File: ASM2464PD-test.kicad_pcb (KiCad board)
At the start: 4 copper layers, 81.8 x 19 mm, 87 parts, among them J1 USB_C_Receptacle, J2 SPIheader, J3 Bus_PCI_Express_x4, U2 SPI_SOIC-8, U3 SPI_DFN-8, Y1 25MHz

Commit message: Very bad routing lol
should probably not try to make it *that* compact
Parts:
- added J4: chip-annoyers, Connector_PinHeader_2.54mm:PinHeader_2x02_P2.54mm_Vertical, F.Cu at (161.5, 60.1)
- added J5: UART, Connector_PinHeader_2.54mm:PinHeader_1x04_P2.54mm_Vertical, F.Cu at (173.2, 50.7)
- added J6: I2C, Connector_PinHeader_2.54mm:PinHeader_1x04_P2.54mm_Vertical, F.Cu at (177.8, 50.7)
- C10, R3, R4, R5, R6: moved to F.Cu
- D1: renamed from D3; moved to F.Cu
- D2: renamed from D4; moved to F.Cu
- D3: renamed from D5; moved to F.Cu
- D4: renamed from D6; moved to F.Cu
- moved R3 161.0 mm to (199.0, 108.0), turned to 180 degrees
- moved R4 160.6 mm to (199.0, 107.0), turned to 180 degrees
- moved R6 154.7 mm to (192.8, 107.6), turned to 180 degrees
- moved R5 154.5 mm to (192.8, 106.6), turned to 180 degrees
- moved R8 148.1 mm to (204.0, 106.0), turned to 180 degrees
- moved R7 148.1 mm to (204.0, 107.0), turned to 180 degrees
- moved C10 126.1 mm to (183.7, 120.8)
- moved R10 81.3 mm to (183.1, 119.2)
- moved R9 81.3 mm to (183.1, 117.4)
- moved Y1 65.4 mm to (172.6, 111.4)
- moved C1 63.4 mm to (172.7, 114.7)
- moved C7 62.2 mm to (190.8, 96.2), turned to 180 degrees
- moved C6 60.6 mm to (190.8, 96.8), turned to 180 degrees
- moved C5 57.6 mm to (190.8, 101.6), turned to 180 degrees
- moved C4 56.9 mm to (190.8, 101.0), turned to 180 degrees
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- renumbered D2 to D10, D7 to D5, D8 to D6, D9 to D7, D10 to D8, D1 to D9
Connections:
- U1 pad H21: unconnected-(U1A-TEST_EN-PadH21) -> TEST_EN
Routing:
- net PCIe_RX3-: track 1.60 -> 36.9 mm, vias 0 -> 1
- net PCIe_RX3+: track 1.66 -> 36.3 mm, vias 0 -> 1
- net /Main/UTX1_C+: track 0.00 -> 18.9 mm, vias 0 -> 2
- net /Main/UTX1_C-: track 0.00 -> 18.9 mm, vias 0 -> 2
- net /Main/URX0_C-: track 0.00 -> 18.8 mm, vias 0 -> 2
- net /Main/URX0_C+: track 0.00 -> 18.8 mm, vias 0 -> 2
- net UTX0-: track 0.00 -> 13.9 mm
- net UTX0+: track 0.00 -> 13.3 mm
- net URX1+: track 0.00 -> 11.9 mm
- net URX1-: track 0.00 -> 11.4 mm
- net /Main/UTX0_C-: track 0.00 -> 7.08 mm
- net /Main/UTX0_C+: track 0.00 -> 7.08 mm
- net URX0-: track 0.00 -> 7.03 mm
- net /Main/URX1_C-: track 0.00 -> 6.92 mm
- net /Main/URX1_C+: track 0.00 -> 6.92 mm
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
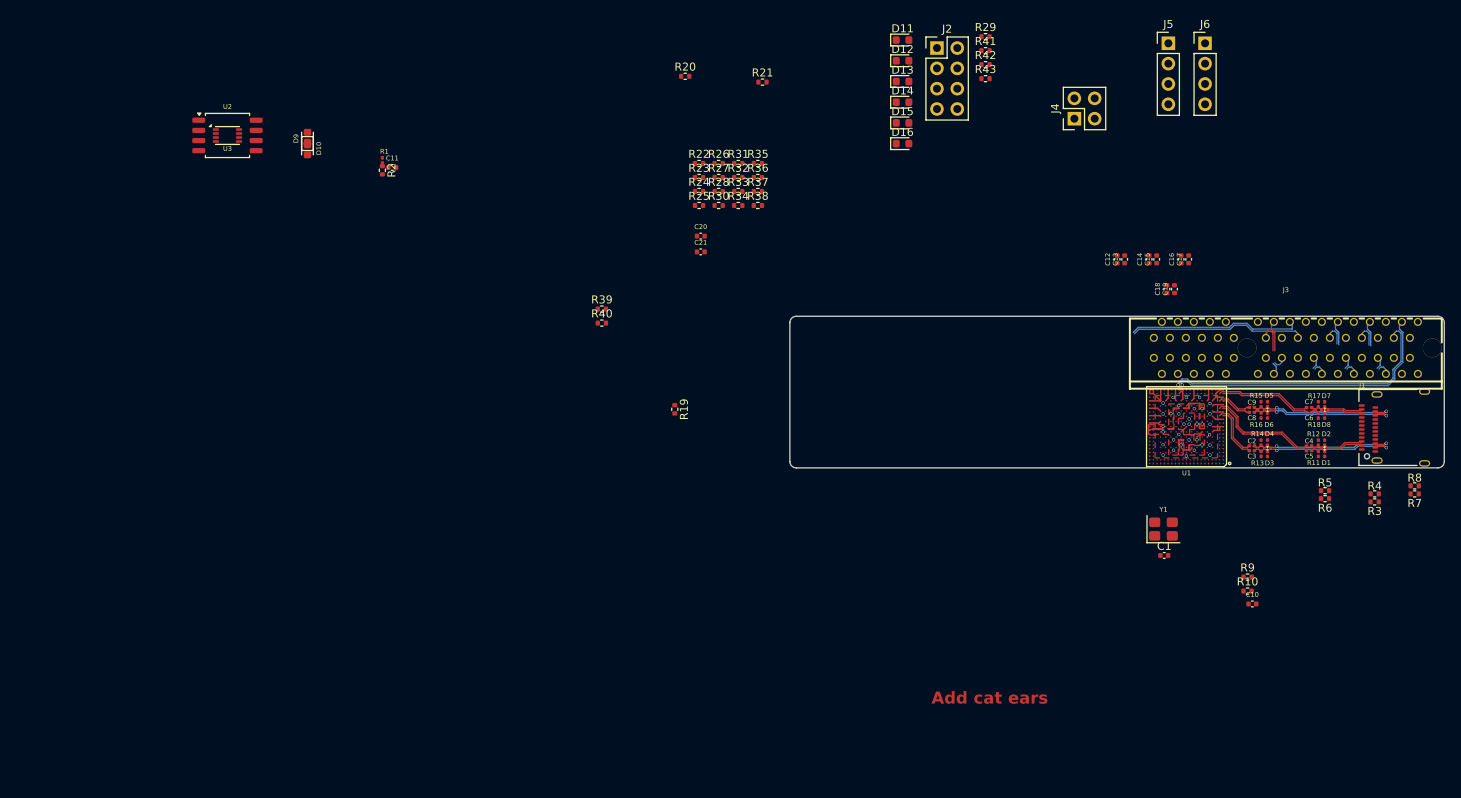
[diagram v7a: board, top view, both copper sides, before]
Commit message: component arrangement
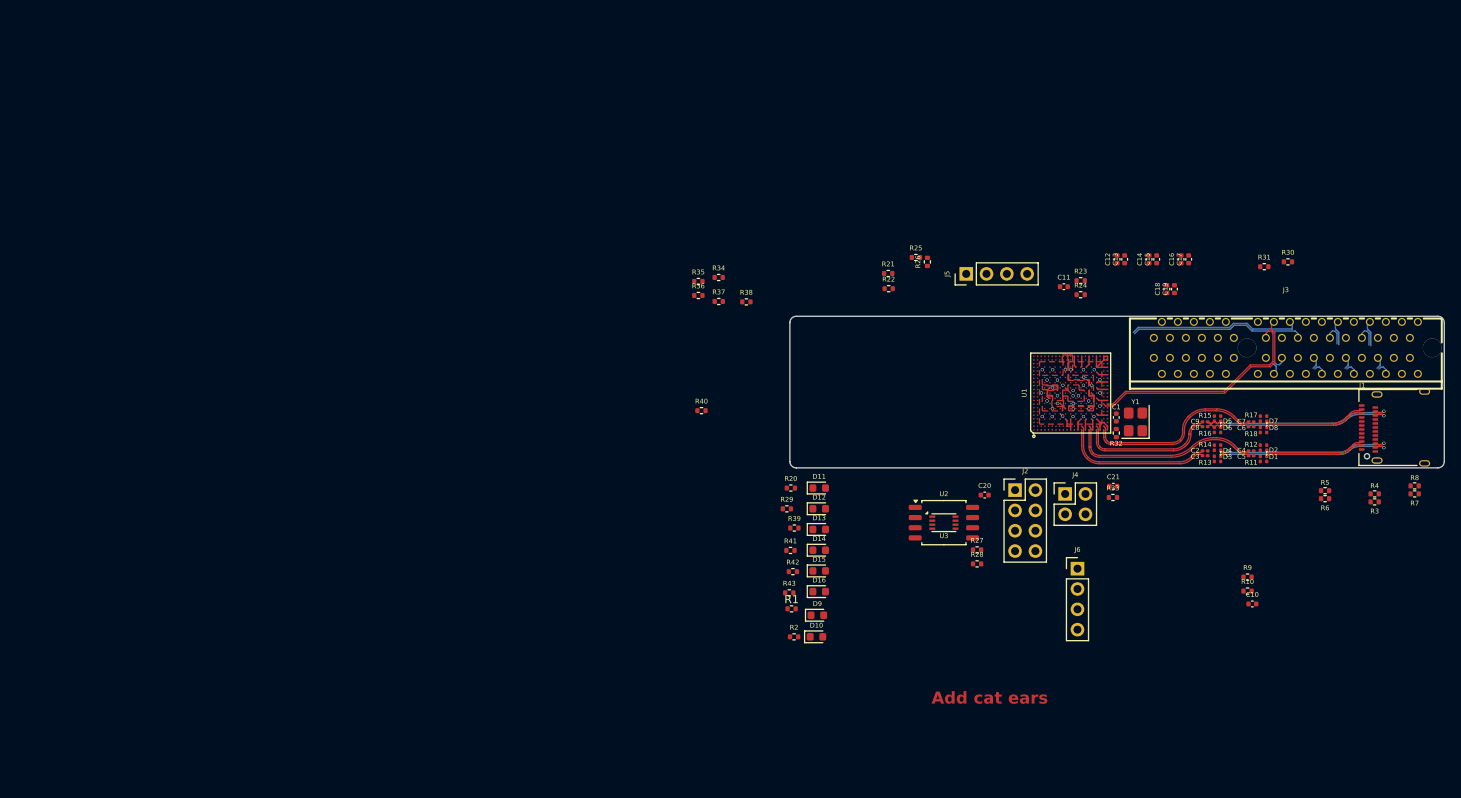
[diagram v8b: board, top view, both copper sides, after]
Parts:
- removed R19: 0Ω, Resistor_SMD:R_0402_1005Metric
- R1: footprint Resistor_SMD:R_0201_0603Metric -> Resistor_SMD:R_0402_1005Metric
- moved U2 101.8 mm to (145.2, 110.6)
- moved U3 101.8 mm to (145.2, 110.6)
- moved D10 88.2 mm to (129.2, 124.9), turned to 0 degrees
- moved D9 87.2 mm to (129.3, 122.2), turned to 0 degrees
- moved C11 85.3 mm to (160.2, 81.1)
- moved R2 77.8 mm to (126.4, 124.9), turned to 0 degrees
- moved R1 75.9 mm to (126.1, 121.4), turned to 0 degrees
- moved R30 71.5 mm to (188.2, 78.0)
- moved R43 68.8 mm to (125.8, 119.4)
- moved R42 67.8 mm to (126.3, 116.7)
- moved J6 67.6 mm to (161.8, 116.3)
- moved R41 67.1 mm to (126.0, 114.1)
- moved R31 67.0 mm to (185.2, 78.6)
- moved R29 64.0 mm to (125.5, 108.9)
- moved R33 60.5 mm to (166.3, 107.5)
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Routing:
- net PCIe_RX3-: track 36.9 -> 0.00 mm, vias 1 -> 0
- net PCIe_RX3+: track 36.3 -> 0.00 mm, vias 1 -> 0
- net REFCLK-: track 3.92 -> 29.1 mm
- net REFCLK+: track 3.87 -> 28.1 mm
- net UTX1-: track 3.85 -> 17.3 mm
- net UTX1+: track 4.40 -> 17.5 mm
- net URX0+: track 6.47 -> 18.8 mm
- net URX0-: track 7.03 -> 19.0 mm
- net URX1-: track 11.4 -> 22.6 mm
- net URX1+: track 11.9 -> 22.8 mm
- net UTX0+: track 13.3 -> 24.0 mm
- net UTX0-: track 13.9 -> 24.1 mm
- net /Main/URX1_C-: track 6.92 -> 12.5 mm
- net /Main/URX1_C+: track 6.92 -> 12.5 mm
- net /Main/UTX0_C+: track 7.08 -> 12.4 mm
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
